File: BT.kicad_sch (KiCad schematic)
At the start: 94 parts, among them J1 Conn_01x05_Pin, J2 Conn_01x03_Pin, J3 S6B-PH-K-S, J4 Boxed_Header_02x03_SMT, K1 AGQ200S12Z, Q1 BSS123, U1 PCM5100A, U2 ESP32-WROOM-32U, U3 TLV4888DR, U4 TLVM23615RDNR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

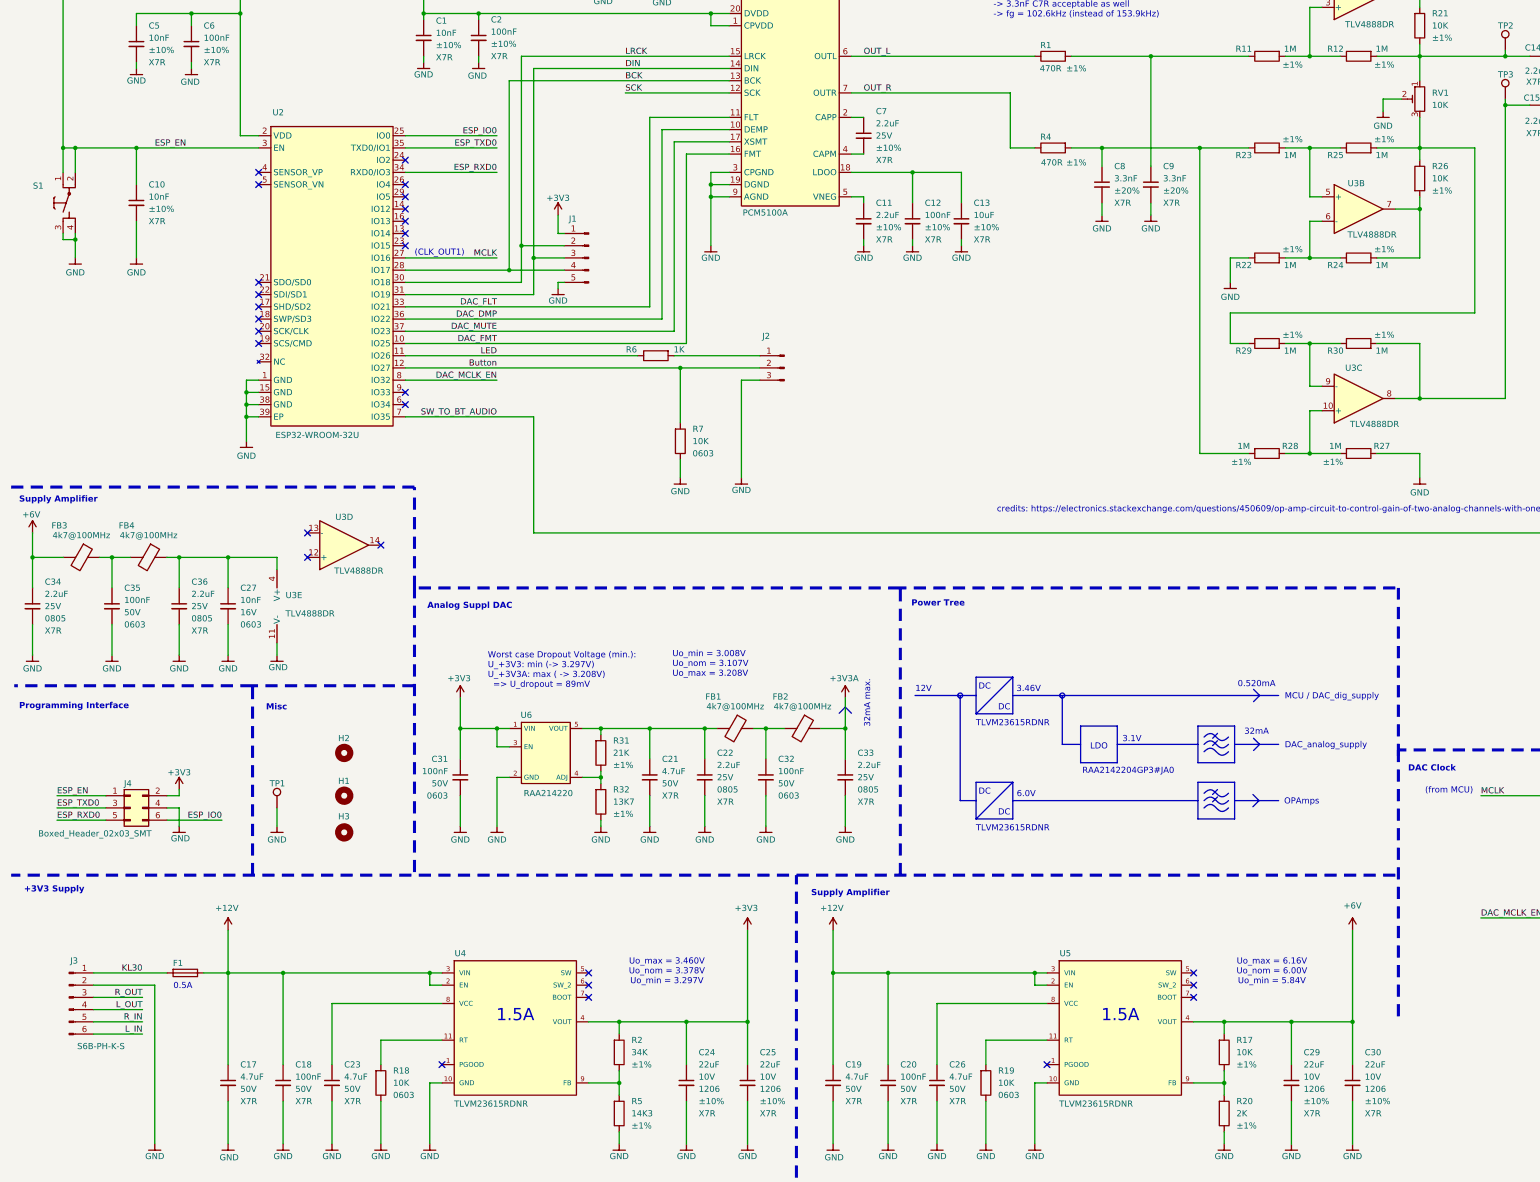
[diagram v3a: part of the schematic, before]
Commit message: rough placement PSU
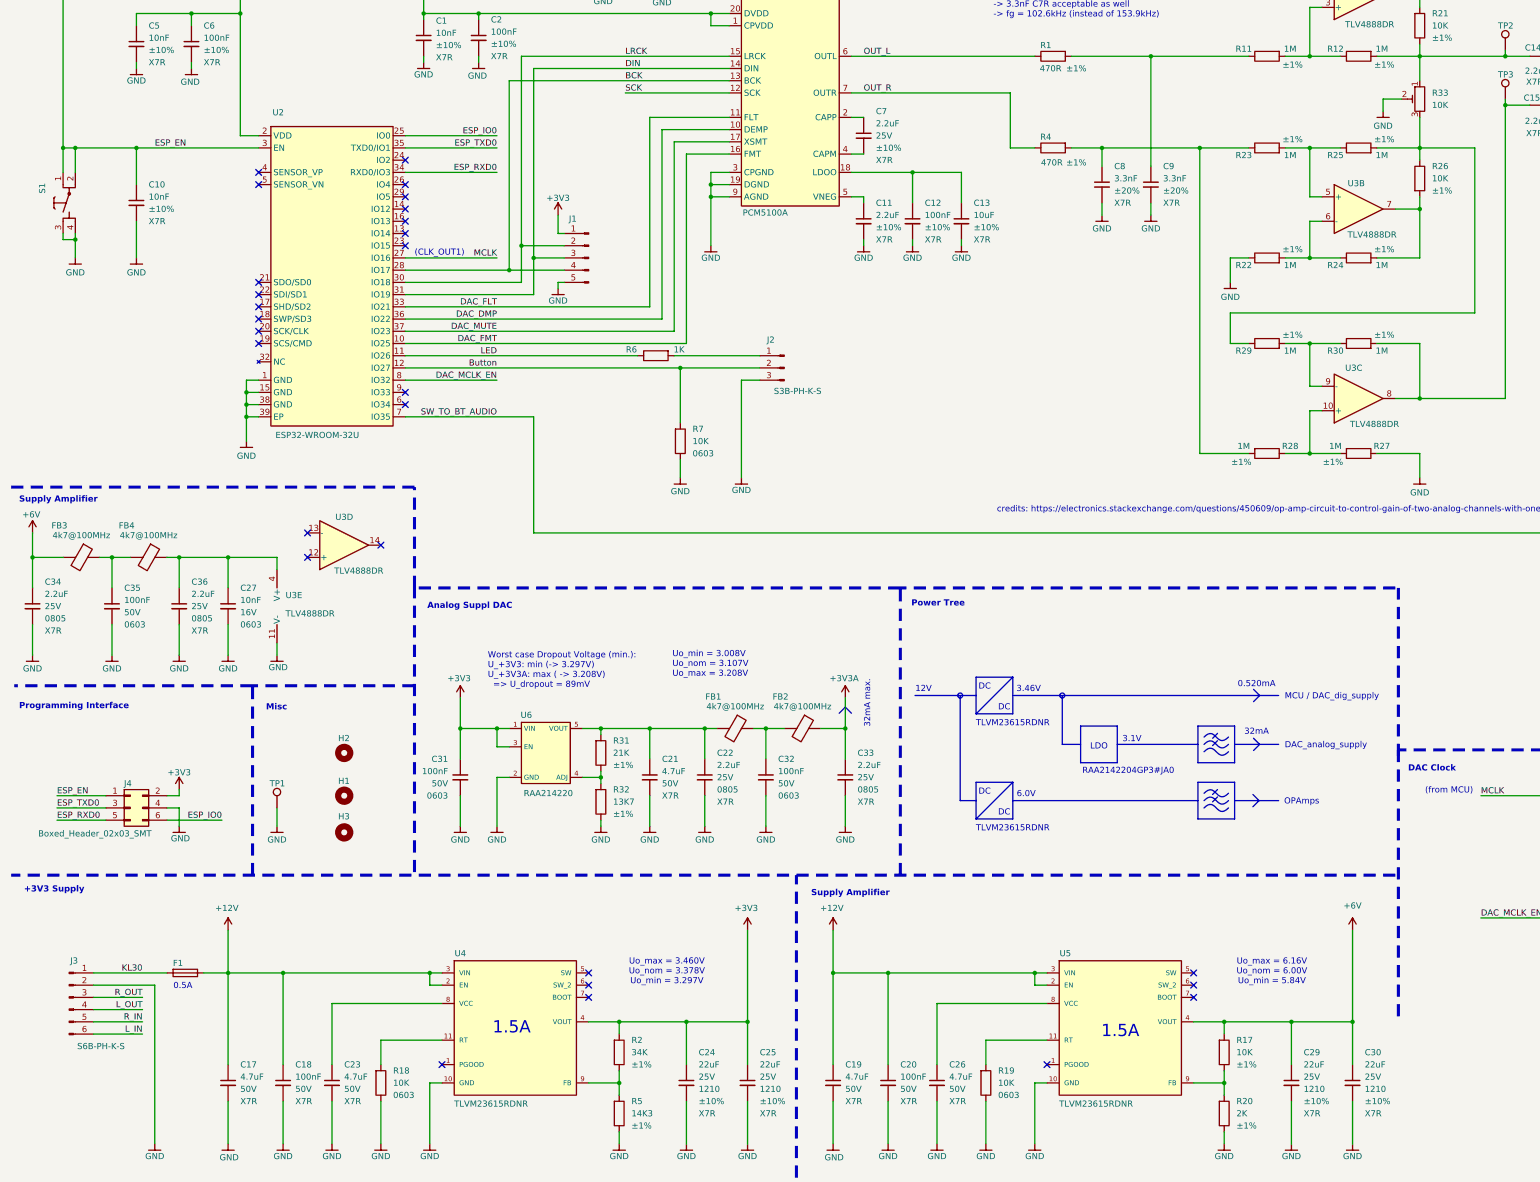
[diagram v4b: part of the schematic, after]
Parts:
- C24, C25, C29, C30: footprint NRD_CAP:C_1206 -> NRD_CAP:C_1210; symbol NRD_C_1206:CL31B226KPHNNNE -> NRD_C_1210:CL32B105KAFNNNE; Manufacturer Part Number CL31B226KPHNNNE -> CL32B105KAFNNNE; Package 1206 -> 1210; Voltage 10V -> 25V; Voltage [V] 10 -> 25
- J2: value Conn_01x03_Pin -> S3B-PH-K-S; footprint (none) -> NRD_CON:S3B-PH-K-S; symbol Connector:Conn_01x03_Pin -> NRD_CON:S3B-PH-K-S; Manufacturer (none) -> JST; Manufacturer Part Number (none) -> S3B-PH-K-S; Maximum Operating Temperature [°C] (none) -> 85; Minimum Operating Temperature [°C] (none) -> -25; RoHS (none) -> Yes
- R33: renamed from RV1; footprint Potentiometer_SMD:Potentiometer_Bourns_TC33X_Vertical -> NRD_R_Var:TC33X-2; symbol Device:R_Potentiometer_Trim -> NRD_R_Var:TC33X-2-103E; Value [Ohm] (none) -> 10e+03
- S1: value (none) -> 434123025826
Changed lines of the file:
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@@
 	(text "1.5A"
 		(exclude_from_sim no)
-		(at 242.57 251.46 0)
+		(at 242.57 254.762 0)
 		(effects
 			(font
@@
 	(text "1.5A"
 		(exclude_from_sim no)
-		(at 116.84 251.46 0)
+		(at 116.078 254 0)
 		(effects
 			(font
@@
 		(dnp no)
 		(property "Reference" "S1"
-			(at 18.796 78.994 90)
+			(at 18.542 79.502 0)
 			(show_name no)
 			(do_not_autoplace no)
@@
 					(size 1.27 1.27)
 				)
-				(justify left)
 			)
 		)
-		(property "Value" ""
-			(at 24.13 82.55 0)
+		(property "Value" "434123025826"
+			(at 21.844 93.472 90)
+			(hide yes)
 			(show_name no)
 			(do_not_autoplace no)
@@
 	)
 	(symbol
-		(lib_id "NRD_C_1206:CL31B226KPHNNNE")
+		(lib_id "NRD_C_1210:CL32B105KAFNNNE")
 		(at 152.4 265.43 0)
 		(unit 1)
@@
 			)
 		)
-		(property "Footprint" "NRD_CAP:C_1206"
+		(property "Footprint" "NRD_CAP:C_1210"
 			(at 152.654 279.908 0)
 			(hide yes)
@@
 			)
 		)
-		(property "Description" "CAP 22uF ±10% 10V X7R 1206"
+		(property "Description" "CAP 22uF ±10% 25V X7R 1210"
 			(at 152.654 279.908 0)
 			(hide yes)
@@
 			)
 		)
-		(property "Manufacturer Part Number" "CL31B226KPHNNNE"
+		(property "Manufacturer Part Number" "CL32B105KAFNNNE"
 			(at 152.654 279.908 0)
 			(hide yes)
@@
 			)
 		)
-		(property "Voltage" "10V"
+		(property "Voltage" "25V"
 			(at 154.94 264.1662 0)
 			(show_name no)
@@
 			)
 		)
-		(property "Voltage [V]" "10"
+		(property "Voltage [V]" "25"
 			(at 147.32 282.194 0)
 			(hide yes)
@@
 			)
 		)
-		(property "Package" "1206"
+		(property "Package" "1210"
 			(at 154.94 266.7062 0)
 			(show_name no)
@@
 	)
 	(symbol
-		(lib_id "Device:R_Potentiometer_Trim")
+		(lib_id "NRD_R_Var:TC33X-2-103E")
 		(at 304.8 60.96 0)
 		(mirror y)
@@
 		(in_pos_files yes)
 		(dnp no)
-		(property "Reference" "RV1"
+		(property "Reference" "R33"
 			(at 307.34 59.6899 0)
 			(show_name no)
@@
 			)
 		)
-		(property "Footprint" "Potentiometer_SMD:Potentiometer_Bourns_TC33X_Vertical"
-			(at 304.8 60.96 0)
-			(hide yes)
-			(show_name no)
-			(do_not_autoplace no)
-			(effects
-				(font
-					(size 1.27 1.27)
-				)
-			)
-		)
-		(property "Datasheet" ""
-			(at 304.8 60.96 0)
-			(hide yes)
-			(show_name no)
-			(do_not_autoplace no)
-			(effects
-				(font
-					(size 1.27 1.27)
-				)
-			)
-		)
-		(property "Description" "Trim-potentiometer"
+		(property "Footprint" "NRD_R_Var:TC33X-2"
 			(at 304.8 60.96 0)
 			(hide yes)
@@
 			)
 		)
-		(property "Sim.Device" "R"
+		(property "Datasheet" "${NERDTRONIX_COMPONENTS_DIR}/Ds/TC33.pdf"
 			(at 304.8 60.96 0)
 			(hide yes)
@@
 			)
 		)
-		(property "Sim.Type" "POT"
+		(property "Description" "Trimme 10k SMT"
 			(at 304.8 60.96 0)
 			(hide yes)
@@
 			)
 		)
-		(property "Sim.Pins" "1=r0 2=wiper 3=r1"
+		(property "Value [Ohm]" "10e+03"
 			(at 304.8 60.96 0)
 			(hide yes)
@@
 			(project "BT"
 				(path "/2a39086a-f2b2-4072-a3e4-22a9fe5f90b0"
-					(reference "RV1")
+					(reference "R33")
 					(unit 1)
 				)
@@
 	)
 	(symbol
-		(lib_id "NRD_C_1206:CL31B226KPHNNNE")
+		(lib_id "NRD_C_1210:CL32B105KAFNNNE")
 		(at 278.13 265.43 0)
 		(unit 1)
@@
 			)
 		)
-		(property "Footprint" "NRD_CAP:C_1206"
+		(property "Footprint" "NRD_CAP:C_1210"
 			(at 278.384 279.908 0)
 			(hide yes)
@@
 			)
 		)
-		(property "Description" "CAP 22uF ±10% 10V X7R 1206"
+		(property "Description" "CAP 22uF ±10% 25V X7R 1210"
 			(at 278.384 279.908 0)
 			(hide yes)
@@
 			)
 		)
-		(property "Manufacturer Part Number" "CL31B226KPHNNNE"
+		(property "Manufacturer Part Number" "CL32B105KAFNNNE"
 			(at 278.384 279.908 0)
 			(hide yes)
@@
 			)
 		)
-		(property "Voltage" "10V"
+		(property "Voltage" "25V"
 			(at 280.67 264.1662 0)
 			(show_name no)
@@
 			)
 		)
-		(property "Voltage [V]" "10"
+		(property "Voltage [V]" "25"
 			(at 273.05 282.194 0)
 			(hide yes)
@@
 			)
 		)
-		(property "Package" "1206"
+		(property "Package" "1210"
 			(at 280.67 266.7062 0)
 			(show_name no)
@@
 	)
 	(symbol
-		(lib_id "NRD_C_1206:CL31B226KPHNNNE")
+		(lib_id "NRD_C_1210:CL32B105KAFNNNE")
 		(at 290.83 265.43 0)
 		(unit 1)
@@
 			)
 		)
-		(property "Footprint" "NRD_CAP:C_1206"
+		(property "Footprint" "NRD_CAP:C_1210"
 			(at 291.084 279.908 0)
 			(hide yes)
@@
 			)
 		)
-		(property "Description" "CAP 22uF ±10% 10V X7R 1206"
+		(property "Description" "CAP 22uF ±10% 25V X7R 1210"
 			(at 291.084 279.908 0)
 			(hide yes)
@@
 			)
 		)
-		(property "Manufacturer Part Number" "CL31B226KPHNNNE"
+		(property "Manufacturer Part Number" "CL32B105KAFNNNE"
 			(at 291.084 279.908 0)
 			(hide yes)
@@
 			)
 		)
-		(property "Voltage" "10V"
+		(property "Voltage" "25V"
 			(at 293.37 264.1662 0)
 			(show_name no)
@@
 			)
 		)
-		(property "Voltage [V]" "10"
+		(property "Voltage [V]" "25"
 			(at 285.75 282.194 0)
 			(hide yes)
@@
 			)
 		)
-		(property "Package" "1206"
+		(property "Package" "1210"
 			(at 293.37 266.7062 0)
 			(show_name no)
@@
 	)
 	(symbol
-		(lib_id "NRD_C_1206:CL31B226KPHNNNE")
+		(lib_id "NRD_C_1210:CL32B105KAFNNNE")
 		(at 165.1 265.43 0)
 		(unit 1)
@@
 			)
 		)
-		(property "Footprint" "NRD_CAP:C_1206"
+		(property "Footprint" "NRD_CAP:C_1210"
 			(at 165.354 279.908 0)
 			(hide yes)
@@
 			)
 		)
-		(property "Description" "CAP 22uF ±10% 10V X7R 1206"
+		(property "Description" "CAP 22uF ±10% 25V X7R 1210"
 			(at 165.354 279.908 0)
 			(hide yes)
@@
 			)
 		)
-		(property "Manufacturer Part Number" "CL31B226KPHNNNE"
+		(property "Manufacturer Part Number" "CL32B105KAFNNNE"
 			(at 165.354 279.908 0)
 			(hide yes)
@@
 			)
 		)
-		(property "Voltage" "10V"
+		(property "Voltage" "25V"
 			(at 167.64 264.1662 0)
 			(show_name no)
@@
 			)
 		)
-		(property "Voltage [V]" "10"
+		(property "Voltage [V]" "25"
 			(at 160.02 282.194 0)
 			(hide yes)
@@
 			)
 		)
-		(property "Package" "1206"
+		(property "Package" "1210"
 			(at 167.64 266.7062 0)
 			(show_name no)
@@
 	)
 	(symbol
-		(lib_id "Connector:Conn_01x03_Pin")
-		(at 172.72 116.84 0)
+		(lib_id "NRD_CON:S3B-PH-K-S")
+		(at 168.91 116.84 0)
 		(mirror y)
 		(unit 1)
@@
 		(dnp no)
 		(property "Reference" "J2"
-			(at 168.148 110.236 0)
+			(at 169.926 110.998 0)
+			(show_name no)
+			(do_not_autoplace no)
+			(effects
+				(font
+					(size 1.27 1.27)
+				)
+			)
+		)
+		(property "Value" "S3B-PH-K-S"
+			(at 175.514 121.666 0)
 			(show_name no)
 			(do_not_autoplace no)
@@
 					(size 1.27 1.27)
 				)
-				(justify right)
 			)
 		)
-		(property "Value" "Conn_01x03_Pin"
-			(at 173.99 118.1099 0)
+		(property "Footprint" "NRD_CON:S3B-PH-K-S"
+			(at 168.91 116.84 0)
 			(hide yes)
 			(show_name no)
@@
 					(size 1.27 1.27)
 				)
-				(justify right)
 			)
 		)
-		(property "Footprint" ""
-			(at 172.72 116.84 0)
+		(property "Datasheet" "${NERDTRONIX_COMPONENTS_DIR}/Ds/JST_PH_Series.pdf"
+			(at 168.91 116.84 0)
 			(hide yes)
 			(show_name no)
@@
 			)
 		)
-		(property "Datasheet" ""
-			(at 172.72 116.84 0)
+		(property "Description" "JST PH Series 01x03 Angled THT"
+			(at 168.91 116.84 0)
+			(hide yes)
+			(show_name no)
+			(do_not_autoplace no)
+			(effects
+				(font
+					(size 1.27 1.27)
+				)
+			)
+		)
+		(property "Minimum Operating Temperature [°C]" "-25"
+			(at 168.91 116.84 0)
+			(hide yes)
+			(show_name no)
+			(do_not_autoplace no)
+			(effects
+				(font
+					(size 1.27 1.27)
+				)
+			)
+		)
+		(property "Maximum Operating Temperature [°C]" "85"
+			(at 168.91 116.84 0)
+			(hide yes)
+			(show_name no)
+			(do_not_autoplace no)
+			(effects
+				(font
+					(size 1.27 1.27)
+				)
+			)
+		)
+		(property "Manufacturer Part Number" "S3B-PH-K-S"
+			(at 168.91 116.84 0)
 			(hide yes)
 			(show_name no)
@@
 			)
 		)
-		(property "Description" "Generic connector, single row, 01x03, script generated"
-			(at 172.72 116.84 0)
+		(property "Manufacturer" "JST"
+			(at 168.91 116.84 0)
+			(hide yes)
+			(show_name no)
+			(do_not_autoplace no)
+			(effects
+				(font
+					(size 1.27 1.27)
+				)
+			)
+		)
+		(property "RoHS" "Yes"
+			(at 168.91 116.84 0)
 			(hide yes)
 			(show_name no)
